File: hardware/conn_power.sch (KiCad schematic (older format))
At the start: 64 parts, among them J201 Conn_02x01, J202 Conn_Coaxial, J203 Conn_Coaxial, J204 Conn_Coaxial, J205 Conn_Coaxial, J206 Conn_Coaxial, J207 Conn_Coaxial, J208 Conn_Coaxial, J209 Conn_Coaxial, J210 Barrel_Jack_Switch, Q201 SI2369DS, U201 LD39100, U205 LM27762

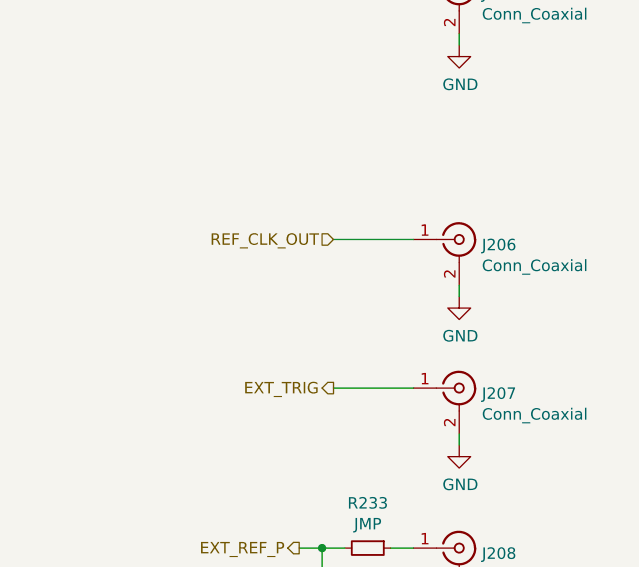
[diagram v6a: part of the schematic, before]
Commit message: finished first pass component placement and drc setup, swapped digital pins for easier routing
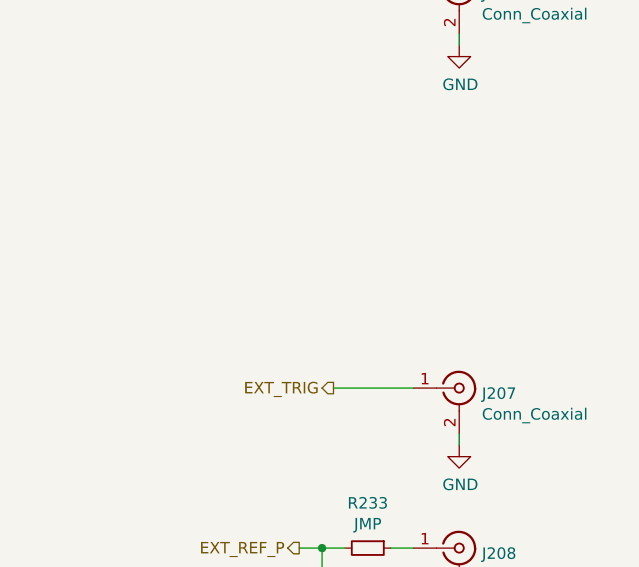
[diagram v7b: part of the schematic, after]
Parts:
- removed J206: Conn_Coaxial, vna_footprints:732511150_sma_thin, symbol Connector:Conn_Coaxial
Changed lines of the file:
@@
 	0    1    1    0
 $EndComp
-Text HLabel 14500 5100 0    50   Input ~ 0
-REF_CLK_OUT
 Text HLabel 13500 4000 0    50   Input ~ 0
 ANALOG_TRIG
@@
 Connection ~ 5700 2650
 $Comp
-L Connector:Conn_Coaxial J206
-U 1 1 5C16C85A
-P 15050 5100
-F 0 "J206" H 15149 5076 50  0000 L CNN
-F 1 "Conn_Coaxial" H 15149 4985 50  0000 L CNN
-F 2 "vna_footprints:732511150_sma_thin" H 15050 5100 50  0001 C CNN
-F 3 " ~" H 15050 5100 50  0001 C CNN
-	1    15050 5100
-	1    0    0    -1
-$EndComp
-$Comp
-L power:GND #PWR0154
-U 1 1 5C16C861
-P 15050 5350
-F 0 "#PWR0154" H 15050 5100 50  0001 C CNN
-F 1 "GND" H 15055 5177 50  0000 C CNN
-F 2 "" H 15050 5350 50  0001 C CNN
-F 3 "" H 15050 5350 50  0001 C CNN
-	1    15050 5350
-	1    0    0    -1
-$EndComp
-Wire Wire Line
-	15050 5350 15050 5300
-Wire Wire Line
-	14850 5100 14500 5100
-$Comp
 L Connector:Conn_Coaxial J205

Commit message: layout of low speed digital traces
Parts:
- R206, R207, R222, R223, R225, R226, R229, R230, R231, R232: footprint Resistors_SMD:R_0402 -> Resistors_SMD:R_0201
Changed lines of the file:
@@
 F 0 "R222" V 13804 3200 50  0000 C CNN
 F 1 "JMP" V 13895 3200 50  0000 C CNN
-F 2 "Resistors_SMD:R_0402" H 14000 3200 50  0001 C CNN
+F 2 "Resistors_SMD:R_0201" H 14000 3200 50  0001 C CNN
 F 3 "~" H 14000 3200 50  0001 C CNN
 	1    14000 3200
@@
 F 0 "R230" V 14304 3200 50  0000 C CNN
 F 1 "JMP" V 14395 3200 50  0000 C CNN
-F 2 "Resistors_SMD:R_0402" H 14500 3200 50  0001 C CNN
+F 2 "Resistors_SMD:R_0201" H 14500 3200 50  0001 C CNN
 F 3 "~" H 14500 3200 50  0001 C CNN
 	1    14500 3200
@@
 F 0 "R225" H 14191 2454 50  0000 R CNN
 F 1 "DNP" H 14191 2545 50  0000 R CNN
-F 2 "Resistors_SMD:R_0402" H 14250 2500 50  0001 C CNN
+F 2 "Resistors_SMD:R_0201" H 14250 2500 50  0001 C CNN
 F 3 "~" H 14250 2500 50  0001 C CNN
 	1    14250 2500
@@
 F 0 "R229" V 14304 2300 50  0000 C CNN
 F 1 "JMP" V 14395 2300 50  0000 C CNN
-F 2 "Resistors_SMD:R_0402" H 14500 2300 50  0001 C CNN
+F 2 "Resistors_SMD:R_0201" H 14500 2300 50  0001 C CNN
 F 3 "~" H 14500 2300 50  0001 C CNN
 	1    14500 2300
@@
 F 0 "R232" H 14491 1054 50  0000 R CNN
 F 1 "DNP" H 14491 1145 50  0000 R CNN
-F 2 "Resistors_SMD:R_0402" H 14550 1100 50  0001 C CNN
+F 2 "Resistors_SMD:R_0201" H 14550 1100 50  0001 C CNN
 F 3 "~" H 14550 1100 50  0001 C CNN
 	1    14550 1100
@@
 F 0 "R223" V 13804 4000 50  0000 C CNN
 F 1 "JMP" V 13895 4000 50  0000 C CNN
-F 2 "Resistors_SMD:R_0402" H 14000 4000 50  0001 C CNN
+F 2 "Resistors_SMD:R_0201" H 14000 4000 50  0001 C CNN
 F 3 "~" H 14000 4000 50  0001 C CNN
 	1    14000 4000
@@
 F 0 "R231" V 14304 4000 50  0000 C CNN
 F 1 "JMP" V 14395 4000 50  0000 C CNN
-F 2 "Resistors_SMD:R_0402" H 14500 4000 50  0001 C CNN
+F 2 "Resistors_SMD:R_0201" H 14500 4000 50  0001 C CNN
 F 3 "~" H 14500 4000 50  0001 C CNN
 	1    14500 4000
@@
 F 0 "R226" H 14191 3404 50  0000 R CNN
 F 1 "DNP" H 14191 3495 50  0000 R CNN
-F 2 "Resistors_SMD:R_0402" H 14250 3450 50  0001 C CNN
+F 2 "Resistors_SMD:R_0201" H 14250 3450 50  0001 C CNN
 F 3 "~" H 14250 3450 50  0001 C CNN
 	1    14250 3450
@@
 F 0 "R207" H 14191 3654 50  0000 R CNN
 F 1 "DNP" H 14191 3745 50  0000 R CNN
-F 2 "Resistors_SMD:R_0402" H 14250 3700 50  0001 C CNN
+F 2 "Resistors_SMD:R_0201" H 14250 3700 50  0001 C CNN
 F 3 "~" H 14250 3700 50  0001 C CNN
 	1    14250 3700
@@
 F 0 "R206" H 14191 2804 50  0000 R CNN
 F 1 "DNP" H 14191 2895 50  0000 R CNN
-F 2 "Resistors_SMD:R_0402" H 14250 2850 50  0001 C CNN
+F 2 "Resistors_SMD:R_0201" H 14250 2850 50  0001 C CNN
 F 3 "~" H 14250 2850 50  0001 C CNN
 	1    14250 2850
